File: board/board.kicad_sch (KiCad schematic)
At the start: 29 parts, among them P1 USB_C_Plug_USB2.0, SW1 BOOTSEL, U1 RP2040, U2 W25Q128JVS, U3 NCP1117-3.3_SOT223, Y1 ABM8-272-T3

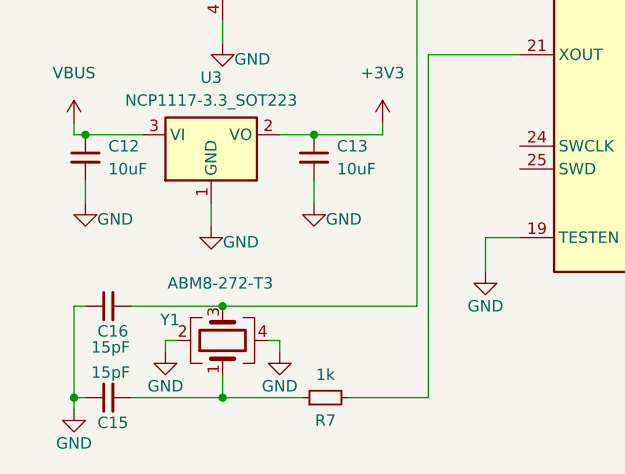
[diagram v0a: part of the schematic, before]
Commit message: switch crystal for a better one
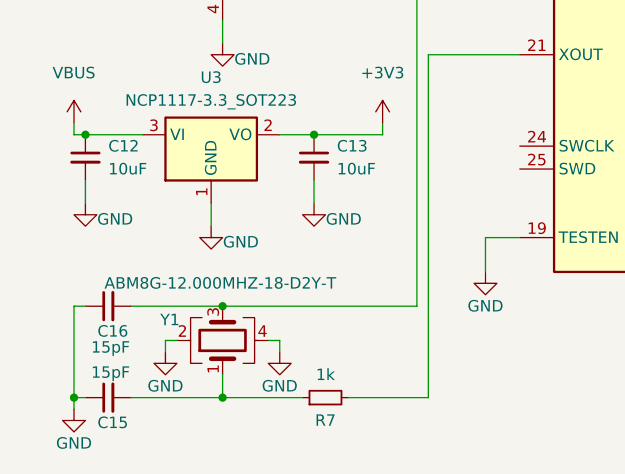
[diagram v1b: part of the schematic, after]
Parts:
- Y1: value ABM8-272-T3 -> ABM8G-12.000MHZ-18-D2Y-T; footprint personal:ABM8-272-T3_ABR -> Crystal:Crystal_SMD_Abracon_ABM8G-4Pin_3.2x2.5mm
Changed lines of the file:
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@@
 			)
 		)
-		(property "Value" "ABM8-272-T3"
+		(property "Value" "ABM8G-12.000MHZ-18-D2Y-T"
 			(at 31.496 133.35 90)
 			(effects
@@
 			)
 		)
-		(property "Footprint" "personal:ABM8-272-T3_ABR"
+		(property "Footprint" "Crystal:Crystal_SMD_Abracon_ABM8G-4Pin_3.2x2.5mm"
 			(at 31.75 139.7 0)
 			(effects

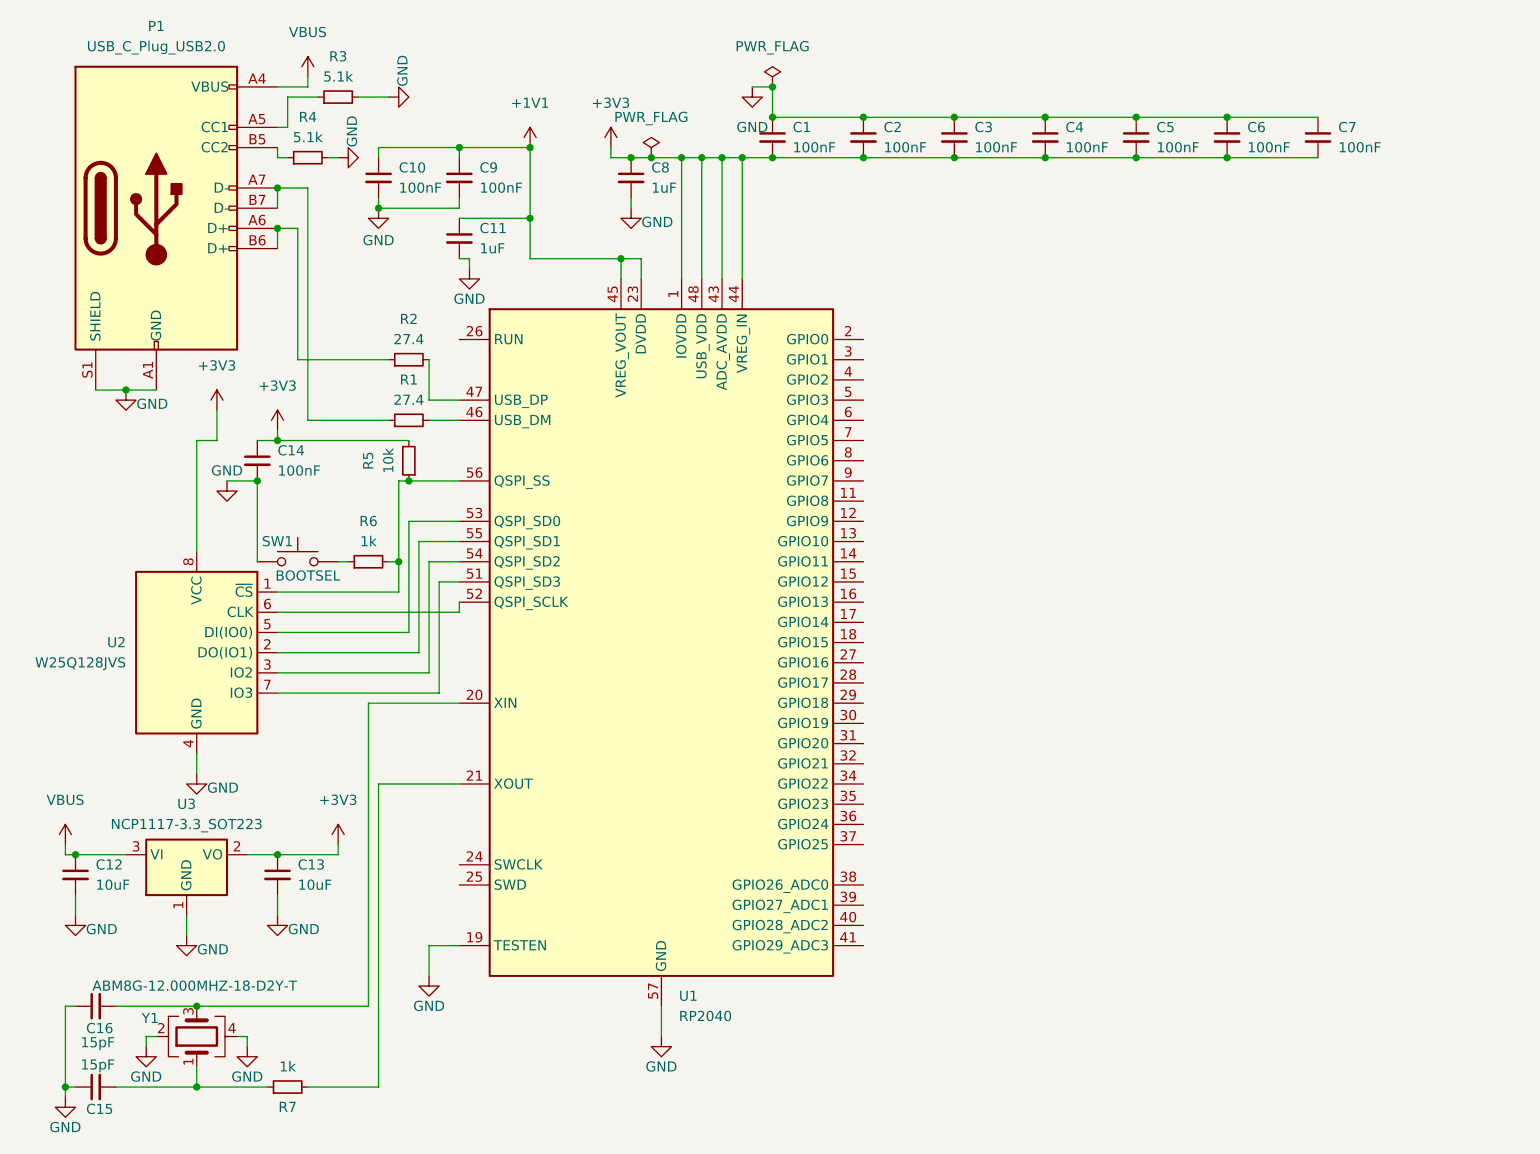
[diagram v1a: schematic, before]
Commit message: Finish LoRa schematic and add RUN button
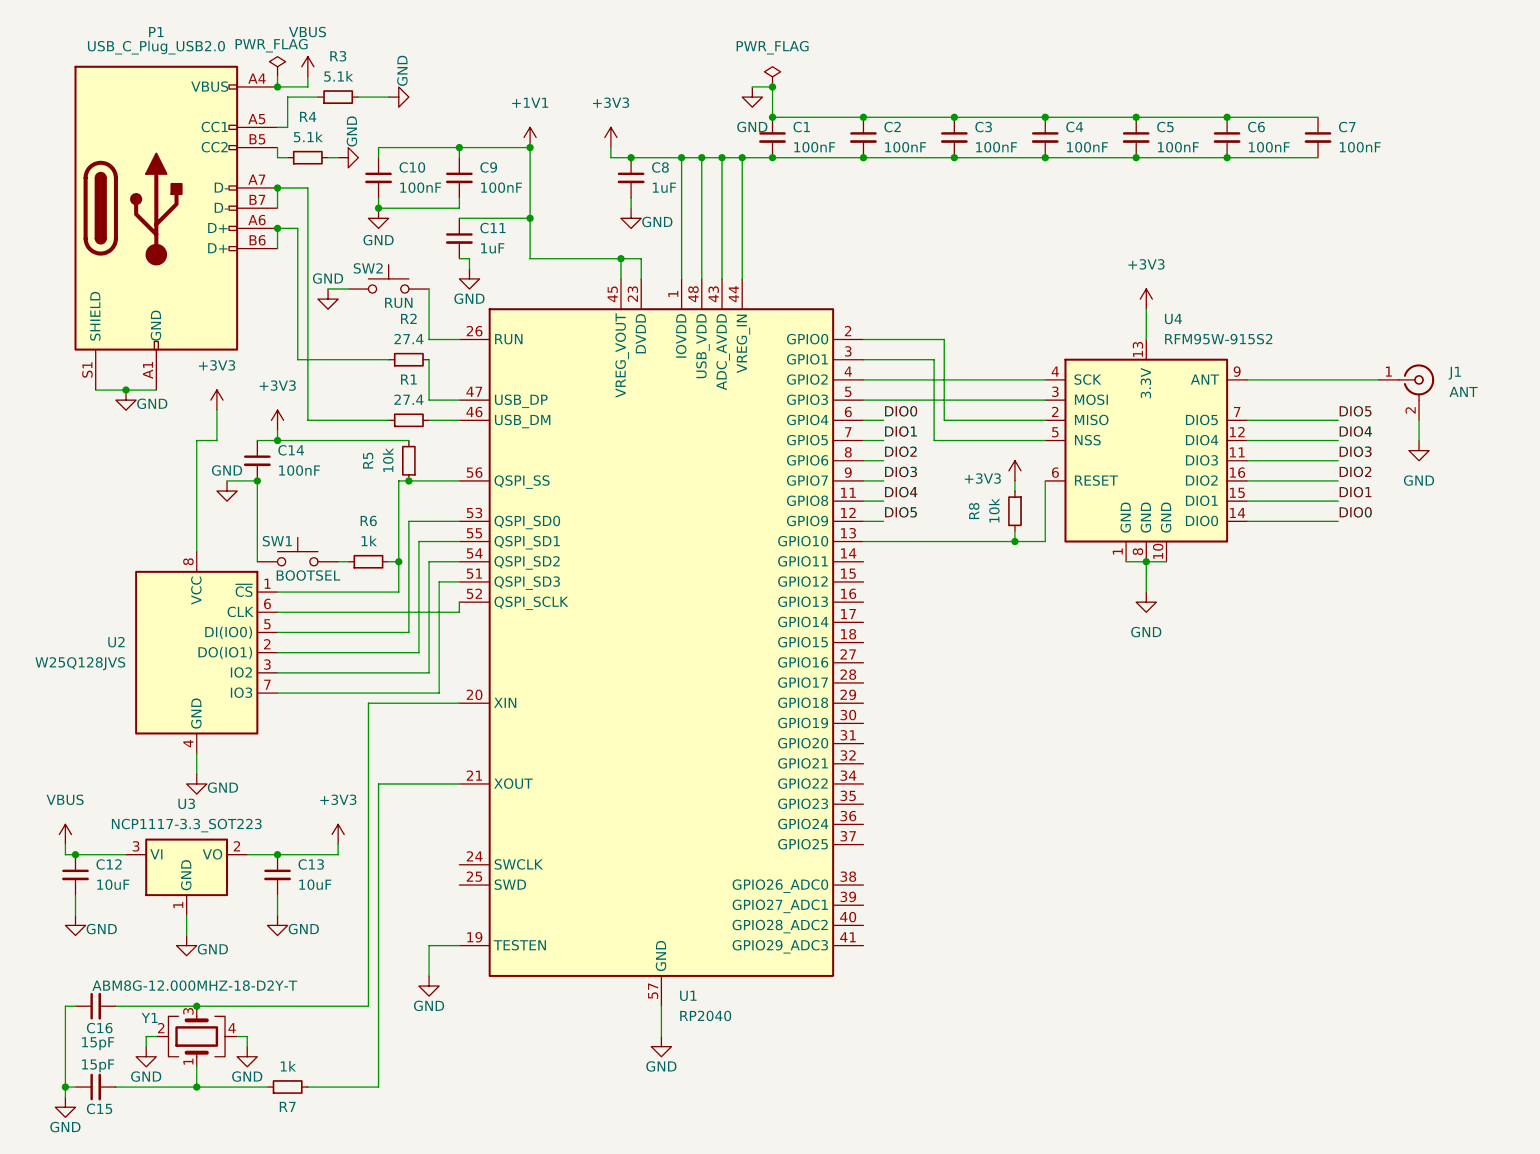
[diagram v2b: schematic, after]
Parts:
- added J1: ANT, Connector_Coaxial:U.FL_Hirose_U.FL-R-SMT-1_Vertical, symbol Connector:Conn_Coaxial
- added R8: 10k, Resistor_SMD:R_0402_1005Metric, symbol Device:R_Small
- added SW2: RUN, Button_Switch_SMD:SW_Push_SPST_NO_Alps_SKRK, symbol Switch:SW_Push
- added U4: RFM95W-915S2, symbol RF_Module:RFM95W-915S2
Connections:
- net +3V3: now also R8.1, U4.13 (3.3V)
- net GND: now also J1.2 (Ext), SW2.1, U4.1 (GND), U4.10 (GND), U4.8 (GND)
- net DIO4: now reaches U1.11 (GPIO8)
- net DIO4: now also U4.12 (DIO4)
- net DIO5: now reaches U1.12 (GPIO9)
- net DIO5: now also U4.7 (DIO5)
- net at U1.13 (GPIO10): now also R8.2, U4.6 (RESET)
- net at U1.2 (GPIO0): now also U4.2 (MISO)
- net at U1.26 (RUN): now also SW2.2
- net at U1.3 (GPIO1): now also U4.5 (NSS)
- net at U1.4 (GPIO2): now also U4.4 (SCK)
- net at U1.5 (GPIO3): now also U4.3 (MOSI)
- net DIO0: now reaches U1.6 (GPIO4)
- net DIO0: now also U4.14 (DIO0)
- net DIO1: now reaches U1.7 (GPIO5)
- net DIO1: now also U4.15 (DIO1)
- net DIO2: now reaches U1.8 (GPIO6)
- net DIO2: now also U4.16 (DIO2)
- net DIO3: now reaches U1.9 (GPIO7)
- net DIO3: now also U4.11 (DIO3)
- new net: J1.1 (In), U4.9 (ANT)

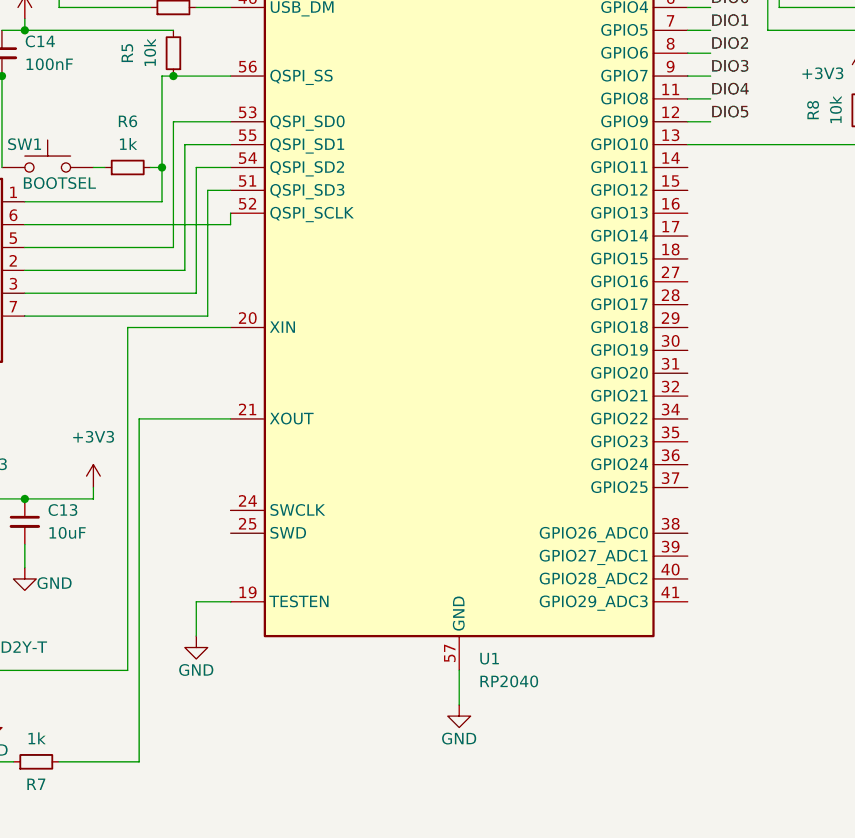
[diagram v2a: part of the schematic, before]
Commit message: Appease ERC and add debug header
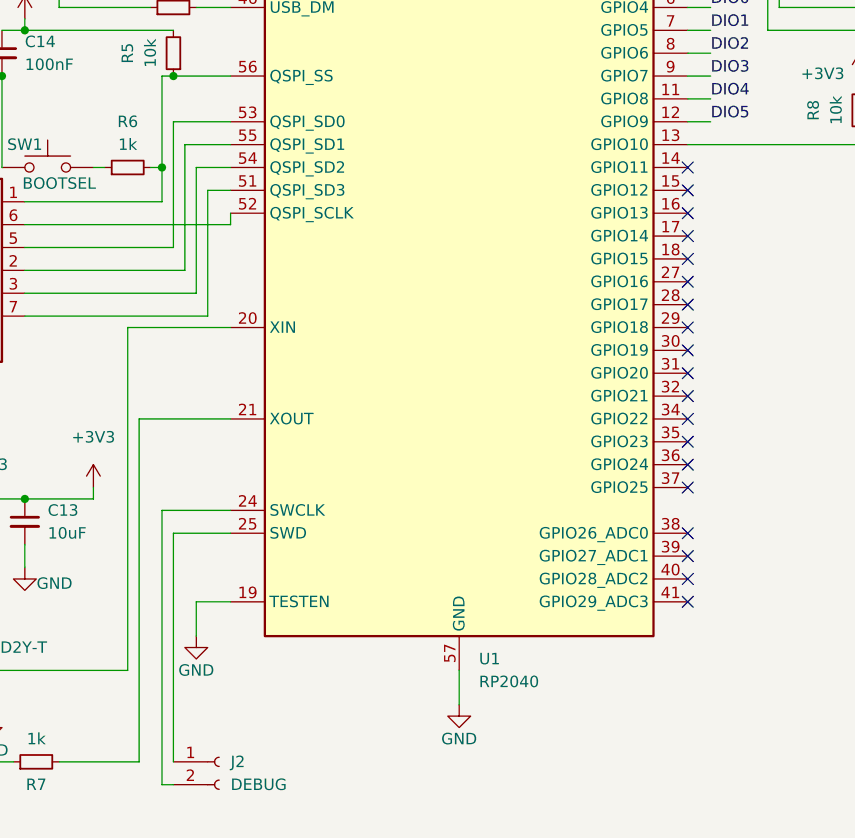
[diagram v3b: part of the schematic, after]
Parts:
- added J2: DEBUG, symbol Connector:Conn_01x02_Socket
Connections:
- net at U1.24 (SWCLK): now also J2.2 (Pin_2)
- net at U1.25 (SWD): now also J2.1 (Pin_1)
- no-connect marks 0 -> 19
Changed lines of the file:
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@@
 		(color 0 0 0 0)
 	)
+	(no_connect
+		(at 115.57 125.73)
+	)
+	(no_connect
+		(at 115.57 128.27)
+	)
+	(no_connect
+		(at 115.57 113.03)
+	)
+	(no_connect
+		(at 115.57 120.65)
+	)
+	(no_connect
+		(at 115.57 87.63)
+	)
+	(no_connect
+		(at 115.57 100.33)
+	)
+	(no_connect
+		(at 115.57 82.55)
+	)
+	(no_connect
+		(at 115.57 102.87)
+	)
+	(no_connect
+		(at 115.57 115.57)
+	)
+	(no_connect
+		(at 115.57 107.95)
+	)
+	(no_connect
+		(at 115.57 85.09)
+	)
+	(no_connect
+		(at 115.57 123.19)
+	)
+	(no_connect
+		(at 115.57 105.41)
+	)
+	(no_connect
+		(at 115.57 97.79)
+	)
+	(no_connect
+		(at 115.57 92.71)
+	)
+	(no_connect
+		(at 115.57 90.17)
+	)
+	(no_connect
+		(at 115.57 80.01)
+	)
+	(no_connect
+		(at 115.57 95.25)
+	)
+	(no_connect
+		(at 115.57 110.49)
+	)
 	(wire
 		(pts
@@
 	(wire
 		(pts
+			(xy 57.15 148.59) (xy 57.15 118.11)
+		)
+		(stroke
+			(width 0)
+			(type default)
+		)
+	)
+	(wire
+		(pts
 			(xy 83.82 27.94) (xy 83.82 29.21)
 		)
@@
 	(wire
 		(pts
+			(xy 57.15 118.11) (xy 64.77 118.11)
+		)
+		(stroke
+			(width 0)
+			(type default)
+		)
+	)
+	(wire
+		(pts
 			(xy 100.33 29.21) (xy 97.79 29.21)
 		)
@@
 	(wire
 		(pts
+			(xy 58.42 120.65) (xy 64.77 120.65)
+		)
+		(stroke
+			(width 0)
+			(type default)
+		)
+	)
+	(wire
+		(pts
 			(xy 31.75 146.05) (xy 40.64 146.05)
 		)
@@
 	(wire
 		(pts
+			(xy 58.42 148.59) (xy 57.15 148.59)
+		)
+		(stroke
+			(width 0)
+			(type default)
+		)
+	)
+	(wire
+		(pts
 			(xy 21.59 135.89) (xy 31.75 135.89)
 		)
@@
 	(wire
 		(pts
+			(xy 58.42 146.05) (xy 58.42 120.65)
+		)
+		(stroke
+			(width 0)
+			(type default)
+		)
+	)
+	(wire
+		(pts
 			(xy 73.66 27.94) (xy 64.77 27.94)
 		)
@@
 					(unit 1)
 				)
+			)
+		)
+	)
+	(symbol
+		(lib_id "Connector:Conn_01x02_Socket")
+		(at 63.5 146.05 0)
+		(unit 1)
+		(exclude_from_sim no)
+		(in_bom yes)
+		(on_board yes)
+		(dnp no)
+		(fields_autoplaced yes)
+		(property "Reference" "J2"
+			(at 64.77 146.0499 0)
+			(effects
+				(font
+					(size 1.27 1.27)
+				)
+				(justify left)
+			)
+		)
+		(property "Value" "DEBUG"
+			(at 64.77 148.5899 0)
+			(effects
+				(font
+					(size 1.27 1.27)
+				)
+				(justify left)
+			)
+		)
+		(property "Footprint" ""
+			(at 63.5 146.05 0)
+			(effects
+				(font
+					(size 1.27 1.27)
+				)
+				(hide yes)
+			)
+		)
+		(property "Datasheet" "~"
+			(at 63.5 146.05 0)
+			(effects
+				(font
+					(size 1.27 1.27)
+				)
+				(hide yes)
+			)
+		)
+		(property "Description" "Generic connector, single row, 01x02, script generated"
+			(at 63.5 146.05 0)
+			(effects
+				(font
+					(size 1.27 1.27)
+				)
+				(hide yes)
+			)
+		)
+		(pin "1"
+		)
+		(pin "2"
+		)
+		(instances
+			(project ""
+				(path "/6eb10beb-f31c-4c13-8f79-f4b6753787bf"
+					(reference "J2")
+					(unit 1)
+				)

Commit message: board design: hr1
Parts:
- J2: footprint (none) -> Connector_PinSocket_2.54mm:PinSocket_1x02_P2.54mm_Vertical
- U4: footprint (none) -> RF_Module:HOPERF_RFM9XW_SMD
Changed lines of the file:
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@@
 			)
 		)
-		(property "Footprint" ""
+		(property "Footprint" "RF_Module:HOPERF_RFM9XW_SMD"
 			(at 67.31 22.86 0)
 			(effects
@@
 			)
 		)
-		(property "Footprint" ""
+		(property "Footprint" "Connector_PinSocket_2.54mm:PinSocket_1x02_P2.54mm_Vertical"
 			(at 63.5 146.05 0)
 			(effects

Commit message: board design: hr2
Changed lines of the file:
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@@
+		)
+	)
+	(label "IOVDD"
+		(at 92.71 29.21 0)
+		(fields_autoplaced yes)
+		(effects
+			(font
+				(size 1.27 1.27)
+			)
+			(justify left bottom)
 		)
 	)
